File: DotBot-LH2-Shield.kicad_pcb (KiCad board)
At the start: 2 copper layers, 33 x 31 mm, 15 parts, among them J1 Conn_01x04, J2 Conn_01x10, J3 Conn_01x10, U1 LSM303AGR, U2 TS4231

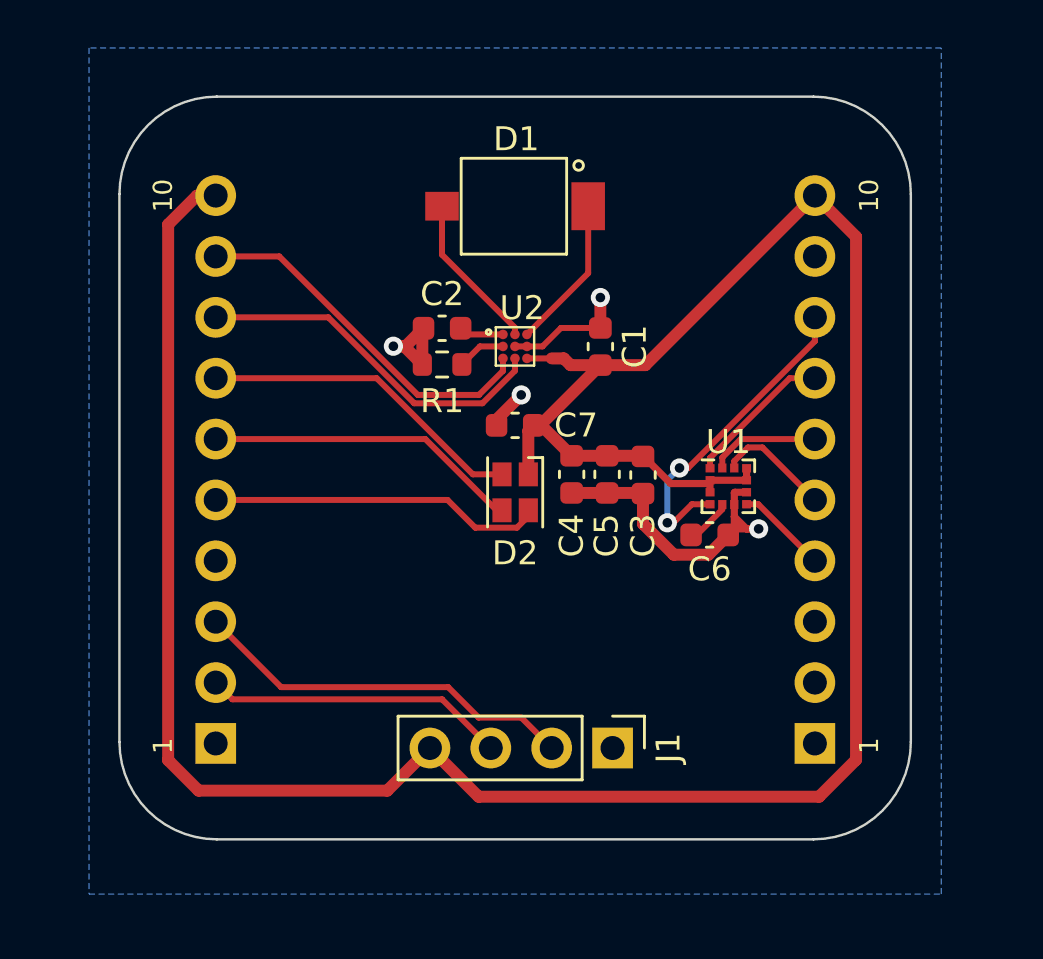
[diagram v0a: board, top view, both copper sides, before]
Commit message: DotBot-LH2-Shield: expose 6V and use it for RGB LED. rework IMU layout abit
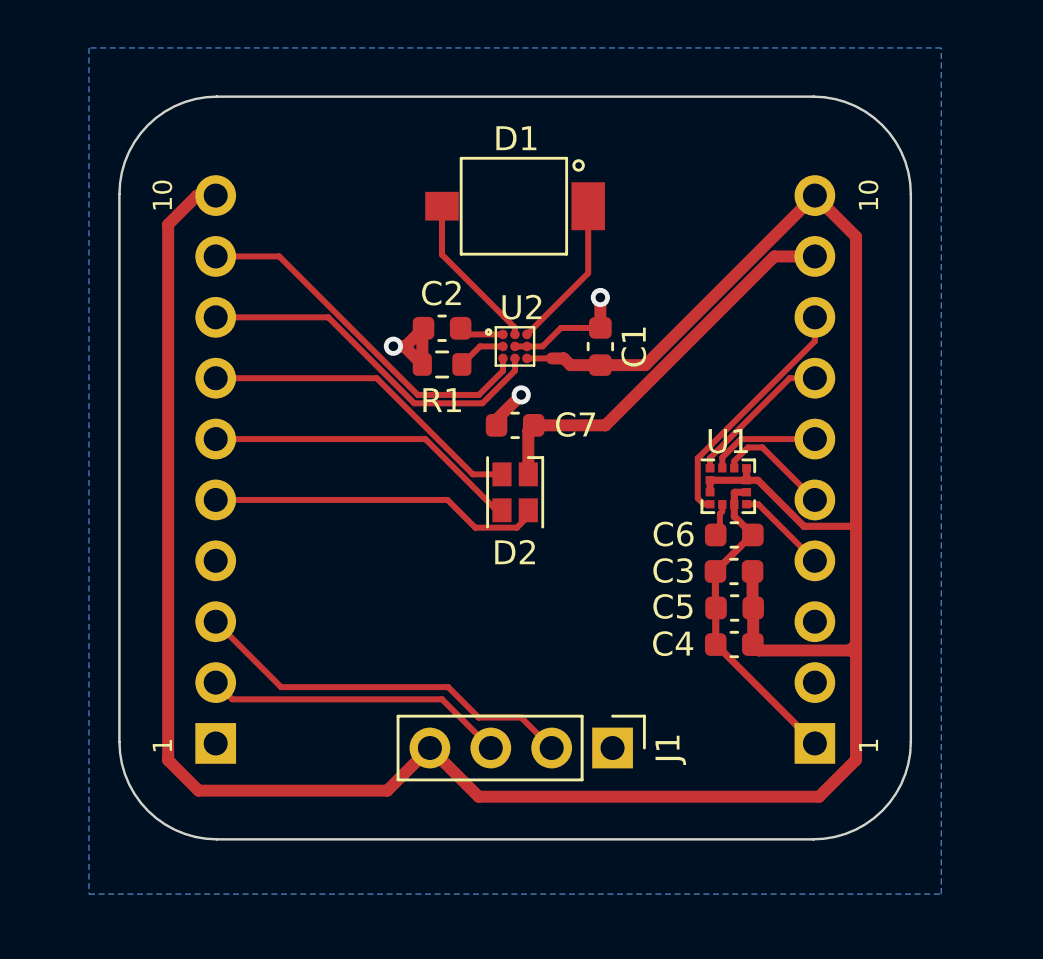
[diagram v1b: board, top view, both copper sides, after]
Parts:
- moved C4 9.82 mm to (151.6, 118.9), turned to 0 degrees
- moved C5 7.71 mm to (151.7, 117.3), turned to 0 degrees
- moved C3 5.53 mm to (151.6, 115.8), turned to 180 degrees
- moved C6 1.03 mm to (151.6, 114.3)
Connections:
- C7 pad 1: +3V3 -> +6V
- D2 pad 1: +3V3 -> +6V
- J3 pad 9: GND -> +6V
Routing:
- net +6V: track 0.00 -> 17.0 mm
- net SDA: track 13.4 -> 10.2 mm, vias 2 -> 0
- net +3V3: track 112.8 -> 111.1 mm
- net Net-(U1-C1): track 1.95 -> 1.38 mm
- net GND: track 24.8 -> 25.2 mm, vias 4 -> 3
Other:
- board text added: "6V"

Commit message: DotBot-LH2-Shield: rework IMU and RGB LED
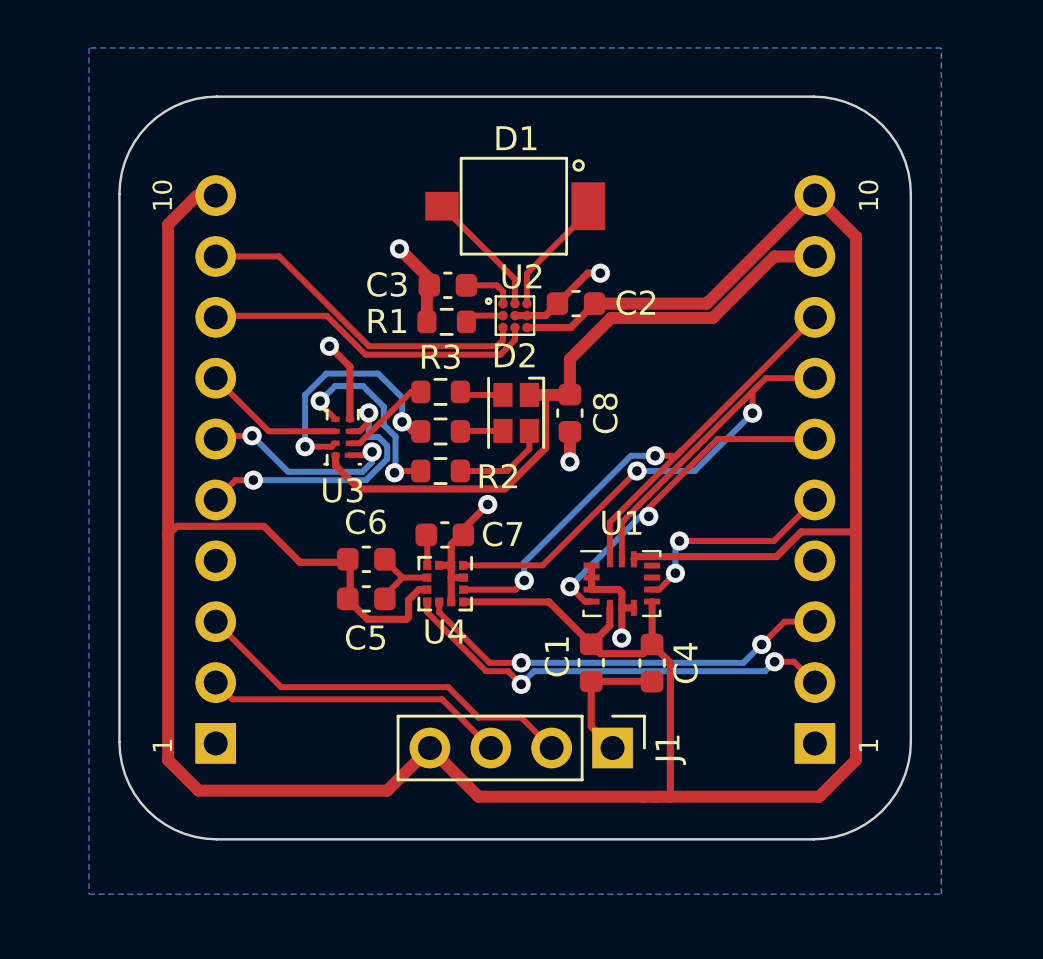
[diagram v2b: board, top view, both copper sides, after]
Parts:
- removed the C3 at (151.6, 115.8)
- removed the C5 at (151.7, 117.3)
- added C1: 100nF, Capacitor_SMD:C_0603_1608Metric, F.Cu at (145.7, 119.6)
- added C7: 100nF, Capacitor_SMD:C_0603_1608Metric, F.Cu at (139.6, 114.3)
- added C8: 100nF, Capacitor_SMD:C_0603_1608Metric, F.Cu at (144.8, 109.2)
- added R2: 240, Resistor_SMD:R_0603_1608Metric, F.Cu at (139.4, 111.6)
- added R3: 470, Resistor_SMD:R_0603_1608Metric, F.Cu at (139.4, 108.3)
- added R4: 261, Resistor_SMD:R_0603_1608Metric, F.Cu at (139.4, 110.0)
- added U3: 74LVC3G34, DotBot:SOT833-1-8_1x1.95_Pitch0.5mm, F.Cu at (135.3, 110.2)
- added U4: LIS3MDL, Package_LGA:LGA-12_2x2mm_P0.5mm, F.Cu at (139.6, 116.3)
- C4: value 10uF -> 100nF
- C6: value 220nF -> 1uF
- U1: value LSM303AGR -> ISM330DHCXTR; footprint Package_LGA:LGA-12_2x2mm_P0.5mm -> Package_LGA:Bosch_LGA-14_3x2.5mm_P0.5mm
- moved C6 15.4 mm to (136.3, 115.3), turned to 0 degrees
- moved C5 9.54 mm to (136.3, 117.0), turned to 0 degrees
- moved U1 6.02 mm to (146.9, 116.3)
- moved C4 3.52 mm to (148.2, 119.6), turned to -90 degrees
- moved D2 3.31 mm to (142.5, 109.2)
- moved C2 2.06 mm to (145.0, 104.6), turned to 0 degrees
- moved C3 1.81 mm to (139.7, 103.9)
- moved R1 1.79 mm to (139.6, 105.4)
- moved U2 1.29 mm to (142.5, 105.1)
- renumbered C1 to C2, C2 to C3, C7 to C5
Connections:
- C4 pad 1: GND -> +3V3
- C4 pad 2: +3V3 -> GND
- C5 pad 1: +6V -> +3V3
- C5 pad 2: GND -> Net-(U4-Vdd)
- C6 pad 1: GND -> +3V3
- C6 pad 2: Net-(U1-C1) -> Net-(U4-Vdd)
- D2 pad 2: LED_R -> Net-(D2-RK)
- D2 pad 3: LED_B -> Net-(D2-BK)
- D2 pad 4: LED_G -> Net-(D2-GK)
- J3 pad 2: unconnected-(J3-Pin_2-Pad2) -> INT
- J3 pad 3: unconnected-(J3-Pin_3-Pad3) -> DRDY
- J3 pad 4: INT_MAG -> unconnected-(J3-Pin_4-Pad4)
- J3 pad 5: INT2_XL -> INT2
- J3 pad 6: INT1_XL -> INT1
- U1 pad 1: SCL -> GND
- U1 pad 10: +3V3 -> unconnected-(U1-OCS_Aux-Pad10)
- U1 pad 11: INT2_XL -> unconnected-(U1-SDO_Aux-Pad11)
- U1 pad 12: INT1_XL -> +3V3
- U1 pad 2: +3V3 -> GND
- U1 pad 3: +3V3 -> GND
- U1 pad 4: SDA -> INT1
- U1 pad 5: Net-(U1-C1) -> +3V3
- U1 pad 7: INT_MAG -> GND
- U1 pad 8: GND -> +3V3
- U1 pad 9: +3V3 -> INT2
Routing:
- net +3V3: track 111.1 -> 138.3 mm
- net SCL: track 6.18 -> 28.0 mm, vias 0 -> 2
- net INT: track 0.00 -> 18.6 mm, vias 0 -> 2
- net DRDY: track 0.00 -> 17.7 mm, vias 0 -> 2
- net SDA: track 10.2 -> 25.5 mm, vias 0 -> 2
- net INT1: track 0.00 -> 14.1 mm, vias 0 -> 2
- net +6V: track 17.0 -> 27.7 mm
- net Net-(R4-Pad1): track 0.00 -> 10.3 mm, vias 0 -> 2
- net INT2: track 0.00 -> 9.03 mm, vias 0 -> 2
- net Net-(R2-Pad1): track 0.00 -> 8.40 mm, vias 0 -> 2
- net LED_G: track 13.6 -> 5.92 mm
- net INT2_XL: track 4.79 -> 0.00 mm
- net INT1_XL: track 4.62 -> 0.00 mm
- net LED_B: track 13.2 -> 9.03 mm, vias 0 -> 2
- net Net-(D2-RK): track 0.00 -> 4.01 mm
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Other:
- board text added: "P0.04"
- board text added: "P0.05"
- board text added: "P0.11/INT"
- board text added: "P1.10"
- board text removed: "P0.04/I_XL2"
- board text removed: "P0.05/I_XL1"
- board text removed: "P0.11"
- board text removed: "P1.10/I_MAG"

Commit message: DotBot-LH2-Shield: improve routing and power planes
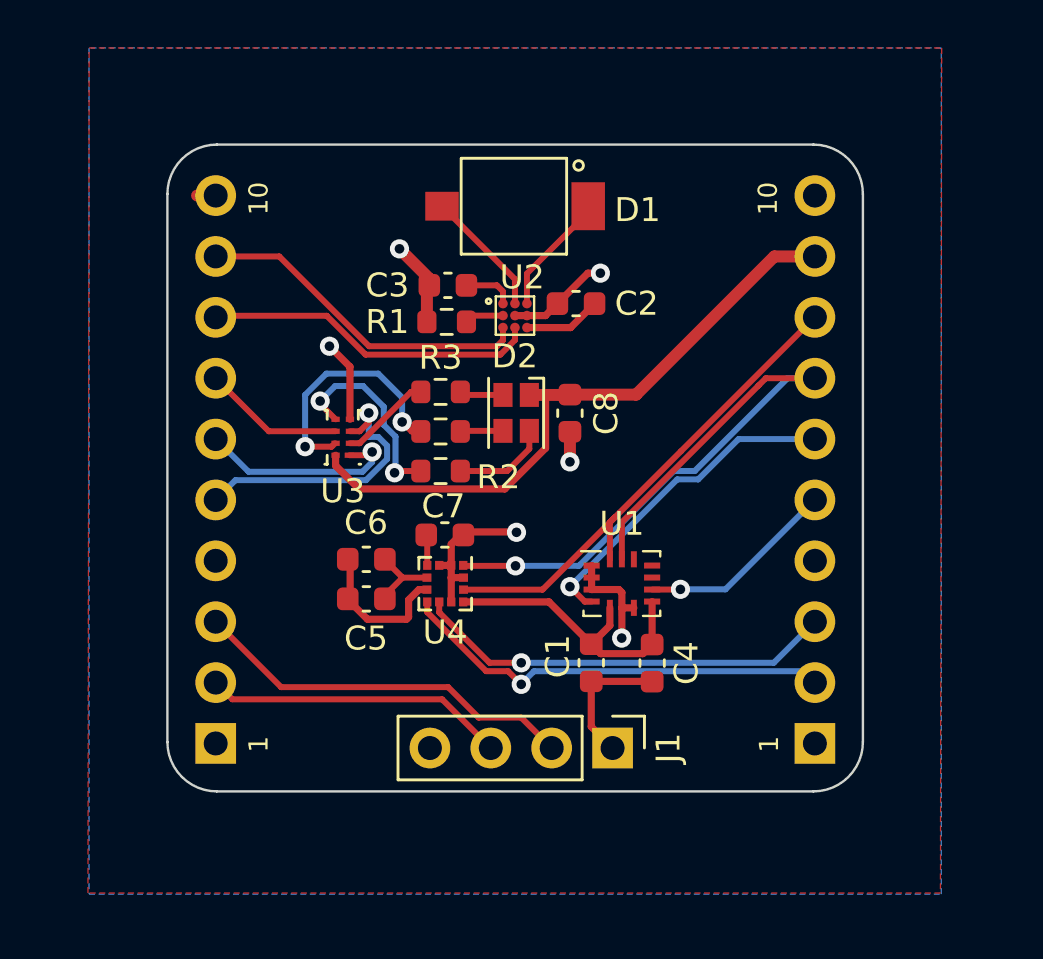
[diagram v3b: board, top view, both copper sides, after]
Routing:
- net +3V3: track 138.3 -> 22.7 mm
- net SDA: track 25.5 -> 21.2 mm, vias 2 -> 0
- net SCL: track 28.0 -> 30.0 mm, vias 2 -> 1
- net +6V: track 27.7 -> 26.8 mm
- net INT2: track 9.03 -> 8.34 mm, vias 2 -> 1
- net GND: track 28.7 -> 29.3 mm
- net LED_B: track 9.03 -> 8.69 mm, vias 2 -> 1
- net INT: track 18.6 -> 18.3 mm, vias 2 -> 1
- net INT1: track 14.1 -> 13.9 mm, vias 2 -> 1
- net LED_R: vias 2 -> 1
- net DRDY: vias 2 -> 1
- added copper zone on F.Cu, net +3V3
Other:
- board size 33 x 31 mm -> 29 x 27 mm

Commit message: switch shield PCB from 2 to 4 layers
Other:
- copper layers 2 -> 4
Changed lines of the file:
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@@
   (layers
     (0 "F.Cu" signal)
+    (1 "In1.Cu" signal)
+    (2 "In2.Cu" signal)
     (31 "B.Cu" power)
     (32 "B.Adhes" user "B.Adhesive")
@@
       (layer "F.Mask" (type "Top Solder Mask") (thickness 0.01))
       (layer "F.Cu" (type "copper") (thickness 0.035))
-      (layer "dielectric 1" (type "core") (thickness 1.51) (material "FR4") (epsilon_r 4.5) (loss_tangent 0.02))
+      (layer "dielectric 1" (type "prepreg") (thickness 0.1) (material "FR4") (epsilon_r 4.5) (loss_tangent 0.02))
+      (layer "In1.Cu" (type "copper") (thickness 0.035))
+      (layer "dielectric 2" (type "core") (thickness 1.24) (material "FR4") (epsilon_r 4.5) (loss_tangent 0.02))
+      (layer "In2.Cu" (type "copper") (thickness 0.035))
+      (layer "dielectric 3" (type "prepreg") (thickness 0.1) (material "FR4") (epsilon_r 4.5) (loss_tangent 0.02))
       (layer "B.Cu" (type "copper") (thickness 0.035))
       (layer "B.Mask" (type "Bottom Solder Mask") (thickness 0.01))

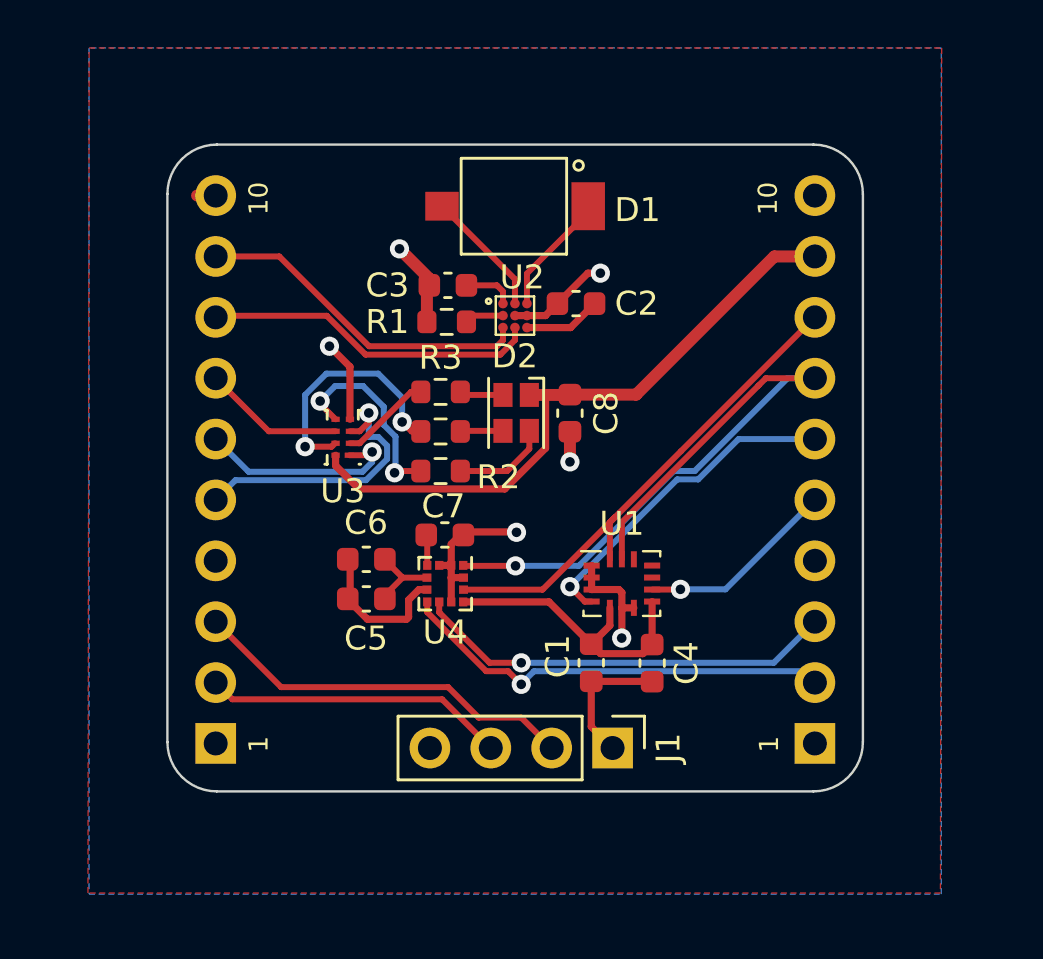
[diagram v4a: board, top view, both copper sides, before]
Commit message: Re-route shield PCB with new LED driver and ground separation
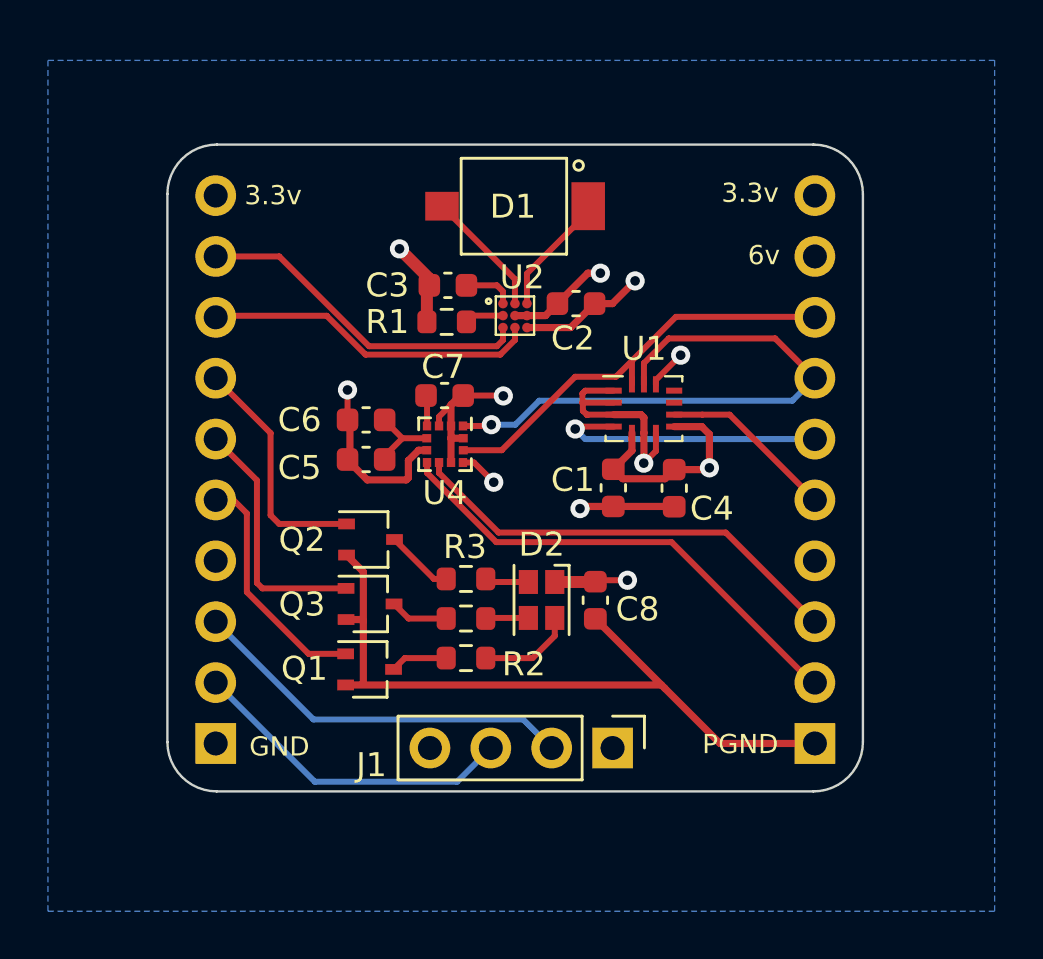
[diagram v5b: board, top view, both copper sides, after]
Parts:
- removed U3: 74LVC3G34, DotBot:SOT833-1-8_1x1.95_Pitch0.5mm
- added Q1: NX6008NBKWX, Package_TO_SOT_SMD:SOT-323_SC-70, F.Cu at (136.4, 119.9)
- added Q2: NX6008NBKWX, Package_TO_SOT_SMD:SOT-323_SC-70, F.Cu at (136.5, 114.5)
- added Q3: NX6008NBKWX, Package_TO_SOT_SMD:SOT-323_SC-70, F.Cu at (136.4, 117.2)
- R2: value 240 -> 1k
- R3: value 470 -> 750
- R4: value 261 -> 750
- moved C8 7.88 mm to (145.8, 117.0)
- moved D2 7.88 mm to (143.6, 117.0)
- moved R2 7.88 mm to (140.4, 119.4)
- moved R4 7.88 mm to (140.4, 117.8)
- moved R3 7.88 mm to (140.4, 116.1)
- moved U1 7.36 mm to (147.9, 109.0)
- moved C1 7.36 mm to (146.6, 112.3)
- moved C4 7.36 mm to (149.1, 112.3)
- moved C5 5.82 mm to (136.3, 111.2)
- moved C6 5.82 mm to (136.3, 109.5)
- moved C7 5.82 mm to (139.6, 108.5)
- moved U4 5.82 mm to (139.6, 110.5)
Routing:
- net GND: track 29.3 -> 59.6 mm, vias 6 -> 5
- net Net-(Q3-D): track 10.3 -> 2.43 mm, vias 2 -> 0
- net Net-(Q1-D): track 8.40 -> 2.39 mm, vias 2 -> 0
- net SCL: track 30.0 -> 24.6 mm
- net +6V: track 26.8 -> 22.5 mm, vias 0 -> 1
- net LED_G: track 5.92 -> 9.99 mm
- net SDA: track 21.2 -> 18.0 mm
- net +3V3: track 22.7 -> 25.1 mm, vias 0 -> 5
- net INT1: track 13.9 -> 11.8 mm
- net INT: track 18.3 -> 20.2 mm, vias 1 -> 0
- net LED_B: track 8.69 -> 10.5 mm, vias 1 -> 0
- net LED_R: track 11.7 -> 10.0 mm, vias 1 -> 0
- net EXT_1: track 12.6 -> 13.8 mm
- net Net-(Q2-D): track 3.84 -> 2.84 mm
- net DRDY: track 17.7 -> 18.7 mm, vias 1 -> 0
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- added copper zone on In2.Cu, net +3V3
- added copper zone on In1.Cu, net GND
- removed copper zone on F.Cu, net +3V3
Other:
- board text added: "3.3v"
- board text added: "6v"
- board text added: "PGND"
- board text removed: "1"
- board text removed: "10"
